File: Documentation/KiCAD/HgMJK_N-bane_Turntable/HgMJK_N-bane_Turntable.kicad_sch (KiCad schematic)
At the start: 7 parts, among them M1 Stepper_Motor_unipolar_5pin, U1 ULN2003

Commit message: file update - KiCAD
New version 1.1
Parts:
- removed D1: LED_Dual_AAK, symbol Device:LED_Dual_AAK
- added D1, D2: LED, symbol Device:LED
- added J1: Screw_Terminal_01x02, symbol Connector:Screw_Terminal_01x02
- added SW2: SW_DPST_x2, symbol Switch:SW_DPST_x2
- R1, R2: value 10K -> 150
- RV1: value R_Potentiometer -> 10K
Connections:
- net +12V: now also M1.1, SW2.2 (B); no longer U1.9 (COM)
- net +5V: now also A1.27 (+5V)
- net GND: now also D1.1 (K), D2.1 (K), J1.2 (Pin_2); no longer RV1.3
- net at R2.1: now also A1.5 (D2); no longer A1.6 (D3)
- net at R2.2: now also D1.2 (A)
- net at R1.1: now also D2.2 (A)
- net at R1.2: now also A1.6 (D3); no longer A1.5 (D2)
- net at U1.13 (O4): now also M1.5
- net at U1.14 (O3): now also M1.4
- net at U1.15 (O2): now also M1.3 (-)
- net at U1.16 (O1): now also M1.2
- new net: J1.1 (Pin_1), SW2.1 (A)
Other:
- note added: "Black"
- note added: "Blue"
- note added: "Brown"
- note added: "Green"
- note added: "Main Power +12VDC"
- note added: "Main Power: +9VDC / +12VDC (max.) GND"
- note added: "ON/OFF"
- note added: "Red"
- note added: "Yellow"
- company: (none) -> EaCode
- title: (none) -> Pot-meter controller for stepMotor
- moved on the sheet: A1, M1, R1, R2, RV1, U1

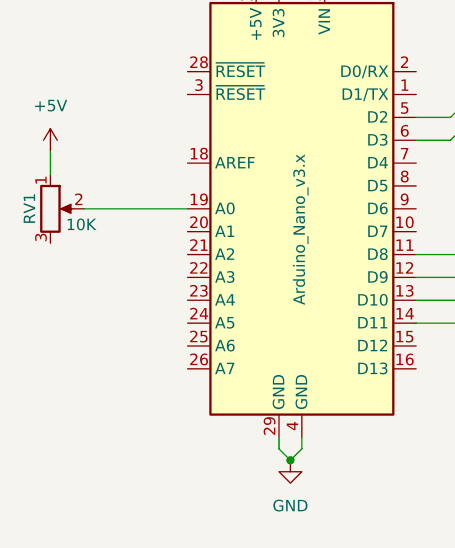
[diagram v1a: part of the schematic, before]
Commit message: file update - KiCAD, main.cpp
Added image of ULN2003 wire connections. edit analogRead values
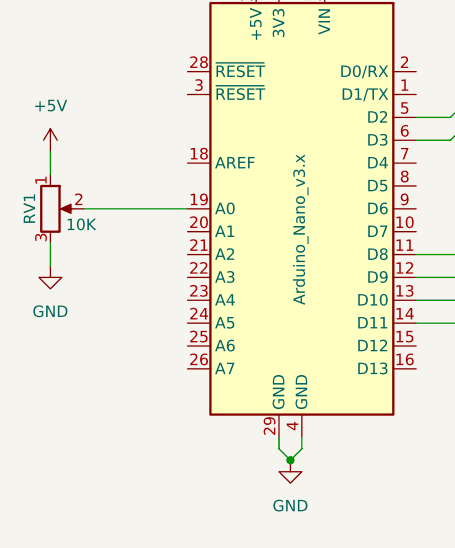
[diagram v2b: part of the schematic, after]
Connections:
- net GND: now also RV1.3
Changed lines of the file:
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@@
+	(wire
+		(pts
+			(xy 85.09 116.84) (xy 85.09 119.38)
+		)
+		(stroke
+			(width 0)
+			(type default)
+		)
+	)
 	(wire
 		(pts
@@
 					(unit 1)
 				)
+			)
+		)
+	)
+	(symbol
+		(lib_id "power:GND")
+		(at 85.09 119.38 0)
+		(unit 1)
+		(exclude_from_sim no)
+		(in_bom yes)
+		(on_board yes)
+		(dnp no)
+		(fields_autoplaced yes)
+		(property "Reference" "#PWR07"
+			(at 85.09 125.73 0)
+			(effects
+				(font
+					(size 1.27 1.27)
+				)
+				(hide yes)
+			)
+		)
+		(property "Value" "GND"
+			(at 85.09 124.46 0)
+			(effects
+				(font
+					(size 1.27 1.27)
+				)
+			)
+		)
+		(property "Footprint" ""
+			(at 85.09 119.38 0)
+			(effects
+				(font
+					(size 1.27 1.27)
+				)
+				(hide yes)
+			)
+		)
+		(property "Datasheet" ""
+			(at 85.09 119.38 0)
+			(effects
+				(font
+					(size 1.27 1.27)
+				)
+				(hide yes)
+			)
+		)
+		(property "Description" "Power symbol creates a global label with name \"GND\" , ground"
+			(at 85.09 119.38 0)
+			(effects
+				(font
+					(size 1.27 1.27)
+				)
+				(hide yes)
+			)
+		)
+		(pin "1"
+		)
+		(instances
+			(project "HgMJK_N-bane_Turntable"
+				(path "/d6299ce4-e04e-4458-87ef-12742b562b87"
+					(reference "#PWR07")
+					(unit 1)
+				)
